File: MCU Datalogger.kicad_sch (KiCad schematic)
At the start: 0 parts

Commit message: add required symbols to the schematics
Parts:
- added BT1: Battery_Cell, symbol Device:Battery_Cell
- added C1, C2, C3, C4: C, symbol Device:C
- added C5: C_Polarized, symbol Device:C_Polarized
- added D1, D2: LED, symbol Device:LED
- added H1, H2, H3, H4: MountingHole, symbol Mechanical:MountingHole
- added R1, R2, R3, R4, R5, R6, R7: R, symbol Device:R
- added U1, U2: 24LC1025, symbol Memory_EEPROM:24LC1025
- added U3: DS1337S_, DS1337S_:SOIC127P600X175-8N, symbol DS1337S_:DS1337S_
- added U4: ATMEGA328P-AU, ATMEGA328P-AU:QFP80P900X900X120-32N, symbol ATMEGA328P-AU:ATMEGA328P-AU
- added Y1, Y2: Crystal, symbol Device:Crystal
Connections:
- new net GND: U4.21 (GND), U4.3 (GND), U4.5 (GND)
- new net VCC: U4.4 (VCC), U4.6 (VCC)
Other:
- added sheet Connectors (Connectors.kicad_sch)
- title: (none) -> ${project_name}

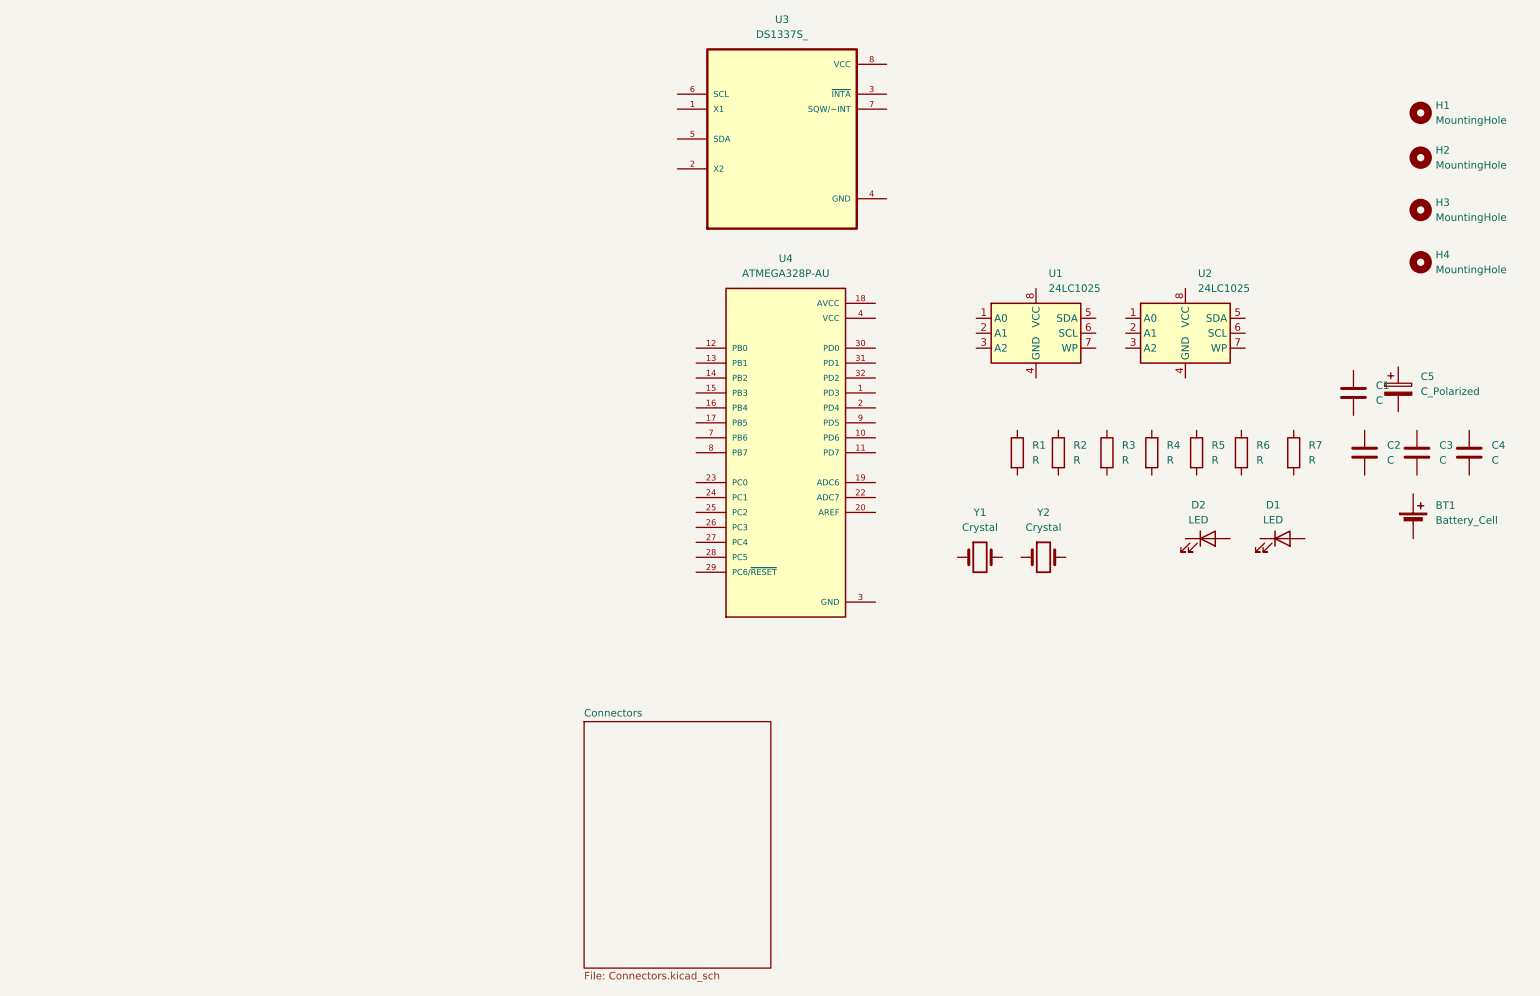
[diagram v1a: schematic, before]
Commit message: add values to symbols
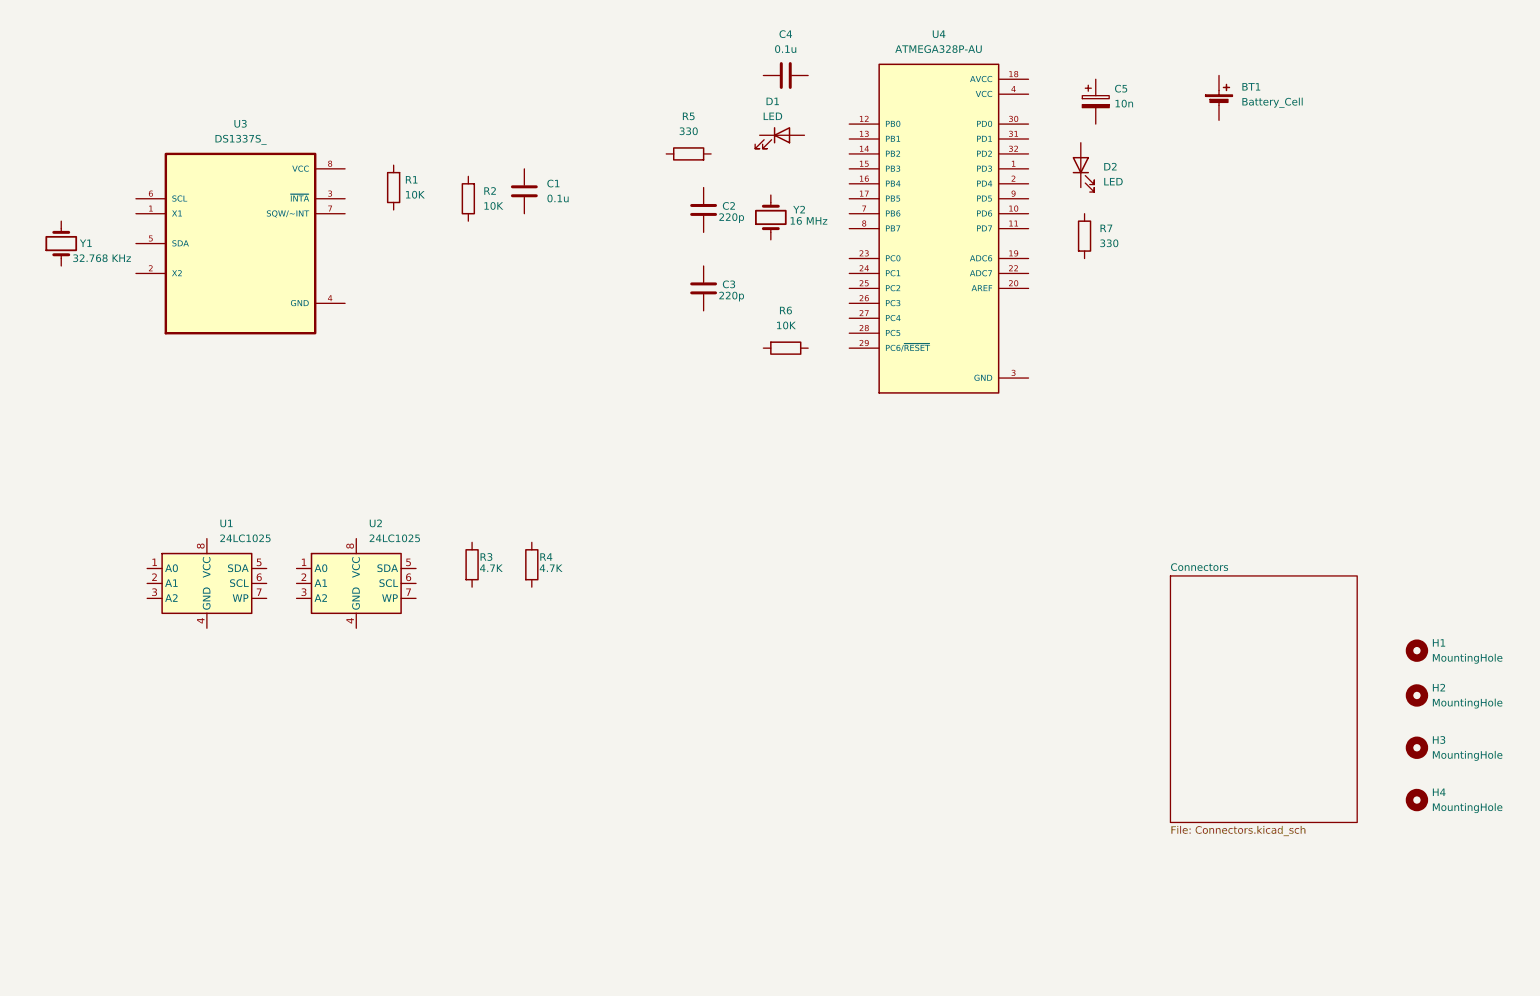
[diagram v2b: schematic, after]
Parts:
- C1, C4: value C -> 0.1u
- C2, C3: value C -> 220p
- C5: value C_Polarized -> 10n
- R1, R2, R6: value R -> 10K
- R3, R4: value R -> 4.7K
- R5, R7: value R -> 330
- Y1: value Crystal -> 32.768 KHz
- Y2: value Crystal -> 16 MHz
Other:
- moved on the sheet: BT1, C1, C2, C3, C4, C5, D1, D2, H1, H2, H3, H4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

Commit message: assign footprints
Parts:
- BT1: footprint (none) -> Connector_PinHeader_2.54mm:PinHeader_1x02_P2.54mm_Vertical
- C1, C2, C3, C4, C5: footprint (none) -> Capacitor_SMD:C_0805_2012Metric
- D1, D2: footprint (none) -> LED_SMD:LED_0805_2012Metric
- H1, H2, H3, H4: footprint (none) -> MountingHole:MountingHole_2.1mm
- R1, R2, R3, R4, R5, R6, R7: footprint (none) -> Resistor_SMD:R_0805_2012Metric
- U1, U2: footprint (none) -> Package_SO:SOIC-8_5.3x5.3mm_P1.27mm
- Y1, Y2: footprint (none) -> Crystal:Crystal_SMD_5032-2Pin_5.0x3.2mm_HandSoldering
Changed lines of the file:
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@@
 			)
 		)
-		(property "Footprint" ""
+		(property "Footprint" "Package_SO:SOIC-8_5.3x5.3mm_P1.27mm"
 			(at 62.865 121.285 0)
 			(hide yes)
@@
 			)
 		)
-		(property "Footprint" ""
+		(property "Footprint" "Resistor_SMD:R_0805_2012Metric"
 			(at 96.393 53.975 90)
 			(hide yes)
@@
 			)
 		)
-		(property "Footprint" ""
+		(property "Footprint" "Capacitor_SMD:C_0805_2012Metric"
 			(at 148.2852 74.93 0)
 			(hide yes)
@@
 			)
 		)
-		(property "Footprint" ""
+		(property "Footprint" "Resistor_SMD:R_0805_2012Metric"
 			(at 116.332 118.11 90)
 			(hide yes)
@@
 			)
 		)
-		(property "Footprint" ""
+		(property "Footprint" "Resistor_SMD:R_0805_2012Metric"
 			(at 109.093 55.88 90)
 			(hide yes)
@@
 			)
 		)
-		(property "Footprint" ""
+		(property "Footprint" "Connector_PinHeader_2.54mm:PinHeader_1x02_P2.54mm_Vertical"
 			(at 234.95 38.481 90)
 			(hide yes)
@@
 			)
 		)
-		(property "Footprint" ""
+		(property "Footprint" "LED_SMD:LED_0805_2012Metric"
 			(at 211.455 50.165 0)
 			(hide yes)
@@
 			)
 		)
-		(property "Footprint" ""
+		(property "Footprint" "LED_SMD:LED_0805_2012Metric"
 			(at 160.655 45.085 0)
 			(hide yes)
@@
 			)
 		)
-		(property "Footprint" ""
+		(property "Footprint" "Capacitor_SMD:C_0805_2012Metric"
 			(at 214.9602 43.18 0)
 			(hide yes)
@@
 			)
 		)
-		(property "Footprint" ""
+		(property "Footprint" "Resistor_SMD:R_0805_2012Metric"
 			(at 106.172 118.11 90)
 			(hide yes)
@@
 			)
 		)
-		(property "Footprint" ""
+		(property "Footprint" "MountingHole:MountingHole_2.1mm"
 			(at 268.605 132.715 0)
 			(hide yes)
@@
 			)
 		)
-		(property "Footprint" ""
+		(property "Footprint" "Capacitor_SMD:C_0805_2012Metric"
 			(at 165.1 33.9598 0)
 			(hide yes)
@@
 			)
 		)
-		(property "Footprint" ""
+		(property "Footprint" "Capacitor_SMD:C_0805_2012Metric"
 			(at 117.8052 58.42 0)
 			(hide yes)
@@
 			)
 		)
-		(property "Footprint" ""
+		(property "Footprint" "Crystal:Crystal_SMD_5032-2Pin_5.0x3.2mm_HandSoldering"
 			(at 158.75 59.055 0)
 			(hide yes)
@@
 			)
 		)
-		(property "Footprint" ""
+		(property "Footprint" "Resistor_SMD:R_0805_2012Metric"
 			(at 144.78 50.038 90)
 			(hide yes)
@@
 			)
 		)
-		(property "Footprint" ""
+		(property "Footprint" "Resistor_SMD:R_0805_2012Metric"
 			(at 161.29 79.502 90)
 			(hide yes)
@@
 			)
 		)
-		(property "Footprint" ""
+		(property "Footprint" "Resistor_SMD:R_0805_2012Metric"
 			(at 210.312 62.23 90)
 			(hide yes)
@@
 			)
 		)
-		(property "Footprint" ""
+		(property "Footprint" "MountingHole:MountingHole_2.1mm"
 			(at 268.605 149.225 0)
 			(hide yes)
@@
 			)
 		)
-		(property "Footprint" ""
+		(property "Footprint" "Capacitor_SMD:C_0805_2012Metric"
 			(at 148.2852 61.595 0)
 			(hide yes)
@@
 			)
 		)
-		(property "Footprint" ""
+		(property "Footprint" "MountingHole:MountingHole_2.1mm"
 			(at 268.605 158.115 0)
 			(hide yes)
@@
 			)
 		)
-		(property "Footprint" ""
+		(property "Footprint" "Package_SO:SOIC-8_5.3x5.3mm_P1.27mm"
 			(at 88.265 121.285 0)
 			(hide yes)
@@
 			)
 		)
-		(property "Footprint" ""
+		(property "Footprint" "Crystal:Crystal_SMD_5032-2Pin_5.0x3.2mm_HandSoldering"
 			(at 38.1 63.5 0)
 			(hide yes)
@@
 			)
 		)
-		(property "Footprint" ""
+		(property "Footprint" "MountingHole:MountingHole_2.1mm"
 			(at 268.605 140.335 0)
 			(hide yes)

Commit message: finish schematic
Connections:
- net GND: now also BT1.2 (-), C1.2, C2.2, C3.2, C4.2, C5.2, R5.2, R7.2, U1.4 (GND), U1.7 (WP), U2.2 (A1), U2.4 (GND), U2.7 (WP), U3.4 (GND)
- net Vcc: now reaches U1.1 (A0)
- net Vcc: now also BT1.1 (+), C1.1, C5.1, D2.2 (A), R1.2, R2.2, R3.1, R4.1, R6.2, U1.2 (A1), U1.3 (A2), U1.8 (VCC), U2.1 (A0), U2.3 (A2), U2.8 (VCC), U3.8 (VCC), U4.18 (AVCC), U4.4 (VCC)
- net SDA: now reaches U1.5 (SDA)
- net SDA: now also R4.2, U2.5 (SDA), U3.5 (SDA), U4.27 (PC4)
- net SCL: now reaches U1.6 (SCL)
- net SCL: now also R3.2, U2.6 (SCL), U3.6 (SCL), U4.28 (PC5)
- net at R1.1: now also U3.3 (~{INTA})
- net at C3.1: now also U4.8 (PB7), Y2.1
- net at R2.1: now also U3.7 (SQW/~INT)
- net at D2.1 (K): now also R7.1
- net D3: now reaches U4.1 (PD3)
- net D6: now reaches U4.10 (PD6)
- net D7: now reaches U4.11 (PD7)
- net D8: now reaches U4.12 (PB0)
- net MOSI: now reaches U4.15 (PB3)
- net MISO: now reaches U4.16 (PB4)
- net SCK: now reaches U4.17 (PB5)
- net SCK: now also D1.2 (A)
- net D4: now reaches U4.2 (PD4)
- net at U4.20 (AREF): now also C4.1
- net RST: now reaches U4.29 (PC6/~{RESET})
- net RST: now also R6.1
- net RX: now reaches U4.30 (PD0)
- net TX: now reaches U4.31 (PD1)
- net D2: now reaches U4.32 (PD2)
- net at U4.7 (PB6): now also C2.1, Y2.2
- net D5: now reaches U4.9 (PD5)
- net at D1.1 (K): now also R5.1
- net at U3.1 (X1): now also Y1.2
- net at U3.2 (X2): now also Y1.1
- net VCC: no longer names the net of U4.6 (VCC)
- net VCC: no longer U4.4 (VCC)
- no-connect marks 0 -> 9
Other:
- sheet Connectors ports: added D2, D3, D4, D5, D6, D7, D8, GND, MISO, MOSI, RST, RX, SCK, SCL, SDA, TX, Vcc; removed none
- note added: "EEPROM"
- note added: "MCU"
- note added: "Mounting"
- note added: "Real time Clock"
- moved on the sheet: BT1, C1, C2, C3, C4, C5, D1, D2, H1, H2, H3, H4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
